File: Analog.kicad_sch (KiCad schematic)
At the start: 18 parts, among them J6 Conn_01x04, U5 LM358

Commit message: cleaned up the whole board
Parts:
- removed C25: 100n, Capacitor_SMD:C_0603_1608Metric_Pad1.08x0.95mm_HandSolder, symbol Device:C_Small
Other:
- moved on the sheet: C24
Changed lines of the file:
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@@
+    (stroke (width 0) (type default))
+  )
+  (wire (pts (xy 184.15 86.36) (xy 184.15 87.63))
+    (stroke (width 0) (type default))
+  )
+  (wire (pts (xy 162.56 143.51) (xy 172.72 143.51))
+    (stroke (width 0) (type default))
+  )
+  (wire (pts (xy 222.25 77.47) (xy 222.25 78.74))
+    (stroke (width 0) (type default))
+  )
+  (wire (pts (xy 189.23 92.71) (xy 187.96 92.71))
+    (stroke (width 0) (type default))
+  )
+  (wire (pts (xy 110.49 149.86) (xy 111.76 149.86))
+    (stroke (width 0) (type default))
+  )
+  (wire (pts (xy 172.72 143.51) (xy 172.72 144.78))
+    (stroke (width 0) (type default))
+  )
+  (wire (pts (xy 69.85 85.09) (xy 74.93 85.09))
+    (stroke (width 0) (type default))
+  )
+  (wire (pts (xy 54.61 85.09) (xy 54.61 86.36))
+    (stroke (width 0) (type default))
+  )
+  (wire (pts (xy 187.96 105.41) (xy 205.74 105.41))
+    (stroke (width 0) (type default))
+  )
+  (wire (pts (xy 162.56 161.29) (xy 172.72 161.29))
+    (stroke (width 0) (type default))
+  )
+  (wire (pts (xy 187.96 92.71) (xy 187.96 105.41))
     (stroke (width 0) (type default))
   )
@@
     (stroke (width 0) (type default))
   )
-  (wire (pts (xy 184.15 86.36) (xy 184.15 87.63))
-    (stroke (width 0) (type default))
-  )
-  (wire (pts (xy 162.56 143.51) (xy 172.72 143.51))
-    (stroke (width 0) (type default))
-  )
-  (wire (pts (xy 154.94 143.51) (xy 162.56 143.51))
-    (stroke (width 0) (type default))
-  )
-  (wire (pts (xy 154.94 161.29) (xy 162.56 161.29))
-    (stroke (width 0) (type default))
-  )
-  (wire (pts (xy 222.25 77.47) (xy 222.25 78.74))
-    (stroke (width 0) (type default))
-  )
-  (wire (pts (xy 189.23 92.71) (xy 187.96 92.71))
-    (stroke (width 0) (type default))
-  )
-  (wire (pts (xy 110.49 149.86) (xy 111.76 149.86))
-    (stroke (width 0) (type default))
-  )
-  (wire (pts (xy 172.72 143.51) (xy 172.72 144.78))
-    (stroke (width 0) (type default))
-  )
-  (wire (pts (xy 69.85 85.09) (xy 74.93 85.09))
-    (stroke (width 0) (type default))
-  )
-  (wire (pts (xy 162.56 143.51) (xy 162.56 149.86))
-    (stroke (width 0) (type default))
-  )
-  (wire (pts (xy 54.61 85.09) (xy 54.61 86.36))
-    (stroke (width 0) (type default))
-  )
-  (wire (pts (xy 187.96 105.41) (xy 205.74 105.41))
-    (stroke (width 0) (type default))
-  )
-  (wire (pts (xy 162.56 161.29) (xy 172.72 161.29))
-    (stroke (width 0) (type default))
-  )
-  (wire (pts (xy 187.96 92.71) (xy 187.96 105.41))
-    (stroke (width 0) (type default))
-  )
-  (wire (pts (xy 154.94 154.94) (xy 154.94 161.29))
-    (stroke (width 0) (type default))
-  )
   (wire (pts (xy 161.29 87.63) (xy 162.56 87.63))
     (stroke (width 0) (type default))
@@
     (stroke (width 0) (type default))
   )
-  (wire (pts (xy 154.94 149.86) (xy 154.94 143.51))
+  (wire (pts (xy 162.56 149.86) (xy 162.56 143.51))
     (stroke (width 0) (type default))
   )
@@
     )
   )
-  (symbol (lib_id "Device:C_Small") (at 154.94 152.4 180) (unit 1)
-    (in_bom yes) (on_board yes) (dnp no)
-    (property "Reference" "C24" (at 156.21 151.13 0)
+  (symbol (lib_id "Device:C_Small") (at 162.56 152.4 180) (unit 1)
+    (in_bom yes) (on_board yes) (dnp no)
+    (property "Reference" "C24" (at 163.83 151.13 0)
       (effects (font (size 1.27 1.27)) (justify right))
     )
-    (property "Value" "100n" (at 156.21 153.67 0)
+    (property "Value" "100n" (at 163.83 153.67 0)
       (effects (font (size 1.27 1.27)) (justify right))
     )
-    (property "Footprint" "Capacitor_SMD:C_0603_1608Metric_Pad1.08x0.95mm_HandSolder" (at 154.94 152.4 0)
-      (effects (font (size 1.27 1.27)) hide)
-    )
-    (property "Datasheet" "~" (at 154.94 152.4 0)
+    (property "Footprint" "Capacitor_SMD:C_0603_1608Metric_Pad1.08x0.95mm_HandSolder" (at 162.56 152.4 0)
+      (effects (font (size 1.27 1.27)) hide)
+    )
+    (property "Datasheet" "~" (at 162.56 152.4 0)
       (effects (font (size 1.27 1.27)) hide)
     )
@@
         )
       )
-    )
-  )
-  (symbol (lib_id "Device:C_Small") (at 162.56 152.4 0) (unit 1)
-    (in_bom yes) (on_board yes) (dnp no) (fields_autoplaced)
-    (property "Reference" "C25" (at 165.1 151.1362 0)
-      (effects (font (size 1.27 1.27)) (justify left))
-    )
-    (property "Value" "100n" (at 165.1 153.6762 0)
-      (effects (font (size 1.27 1.27)) (justify left))
-    )
-    (property "Footprint" "Capacitor_SMD:C_0603_1608Metric_Pad1.08x0.95mm_HandSolder" (at 162.56 152.4 0)
-      (effects (font (size 1.27 1.27)) hide)
-    )
-    (property "Datasheet" "~" (at 162.56 152.4 0)
-      (effects (font (size 1.27 1.27)) hide)
-    )
-    (pin "1")
-    (pin "2")
-    (instances
-      (project "Apollo - DSP"
-        (path "/e63e39d7-6ac0-4ffd-8aa3-1841a4541b55/b09314ce-9d59-4e3d-844f-f36b76e34219"
-          (reference "C25") (unit 1)
-        )
-      )

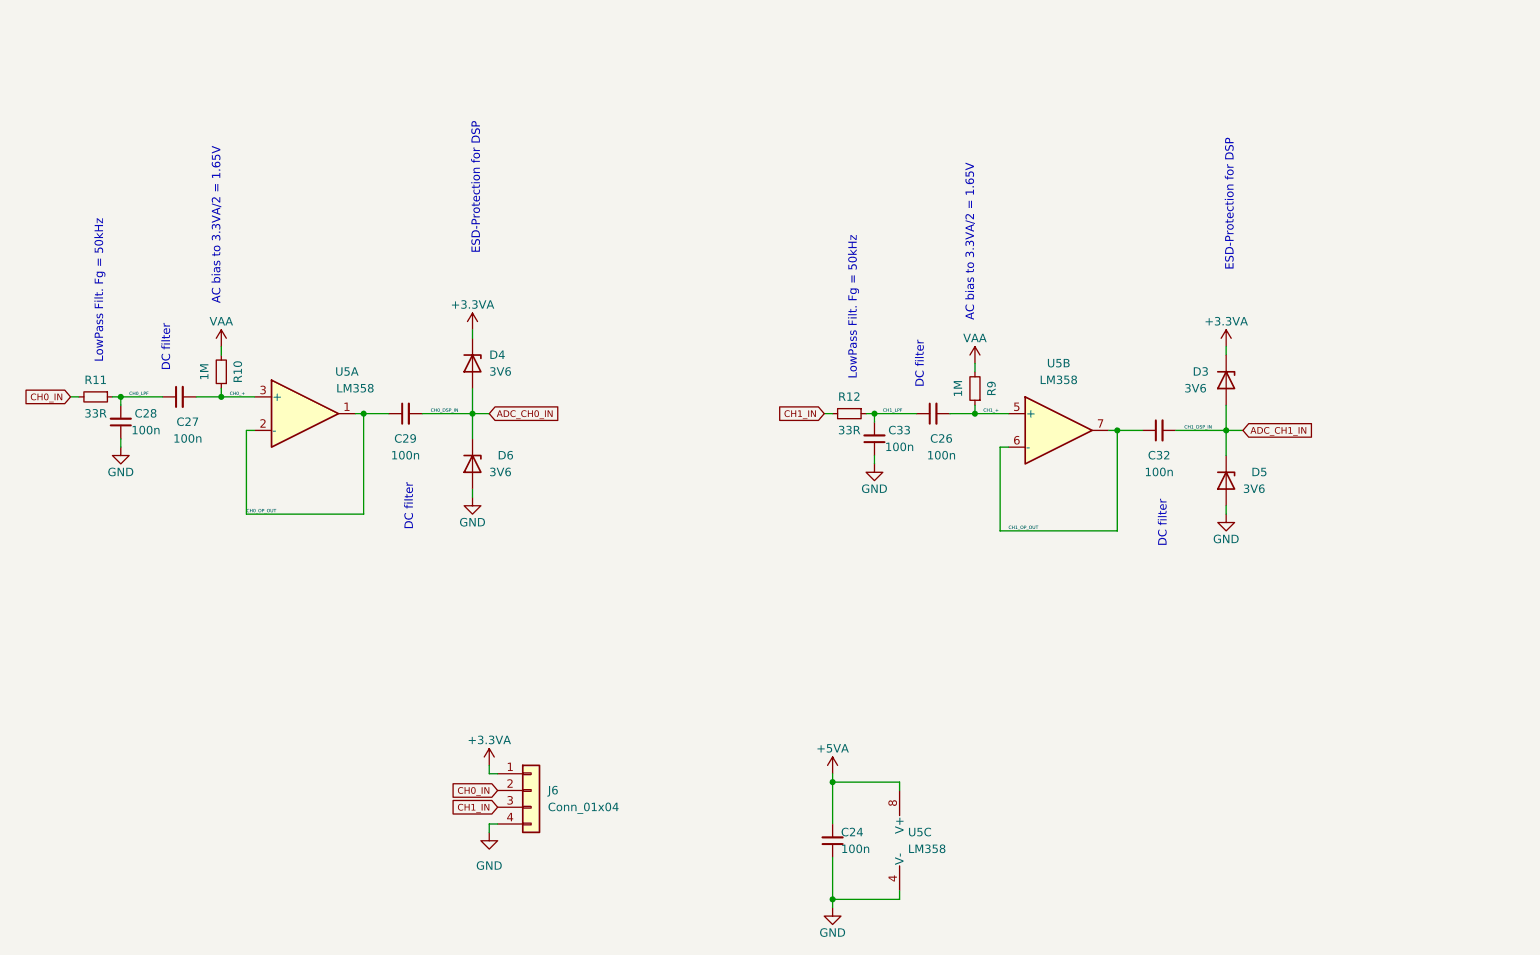
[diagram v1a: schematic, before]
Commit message: made analog circuitry a bit more compact moved whole board
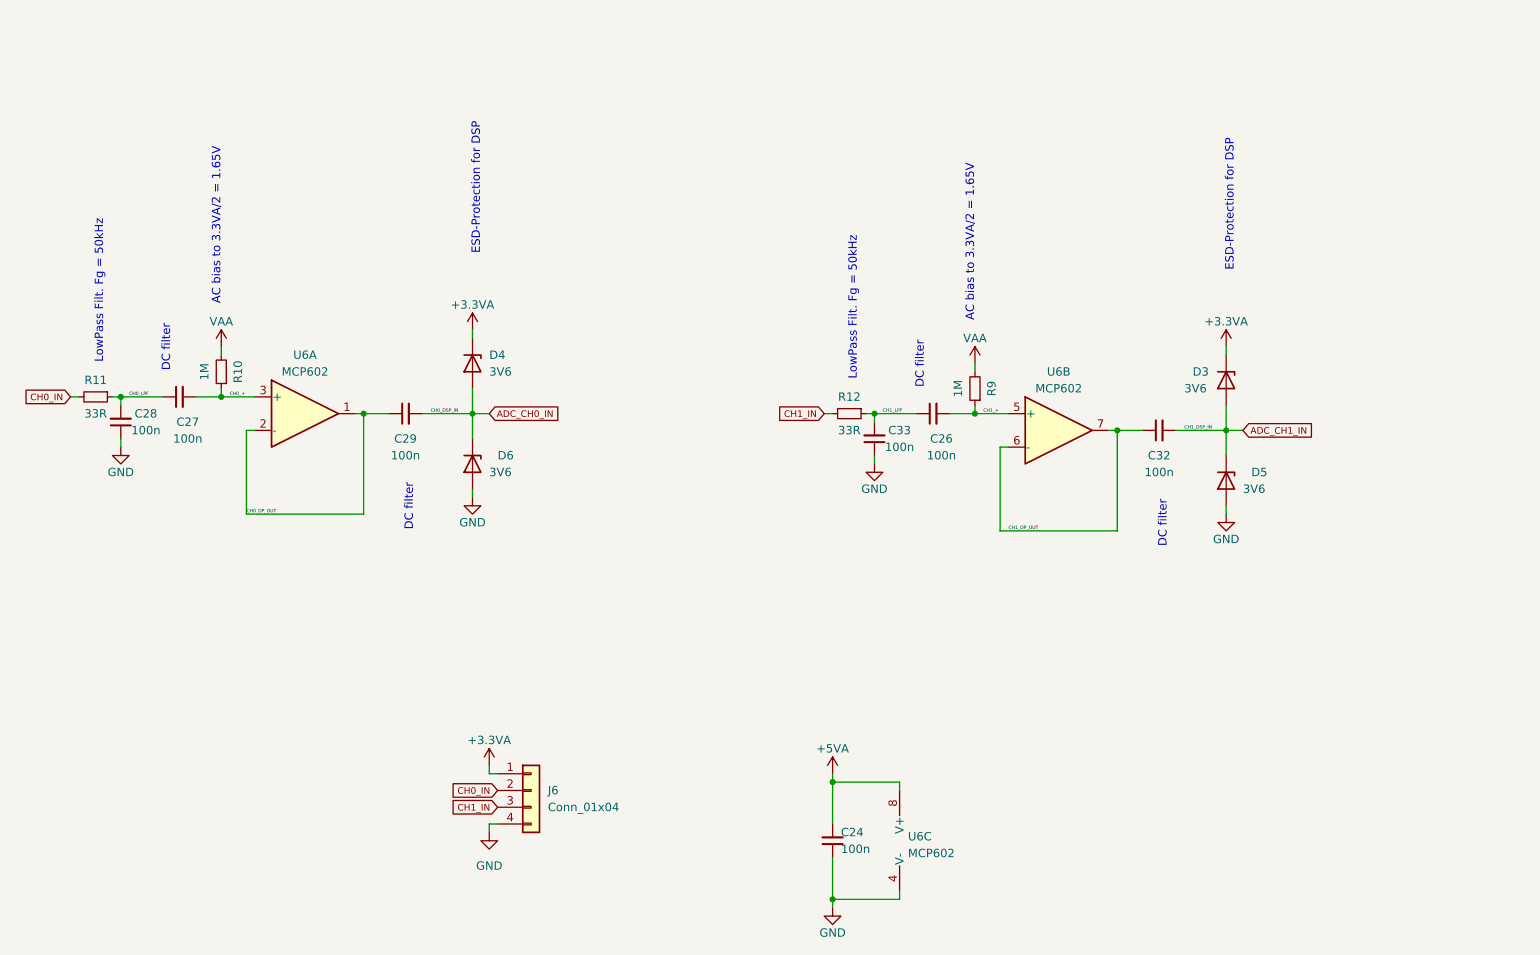
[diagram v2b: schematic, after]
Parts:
- removed U5: LM358, Package_SO:SOIC-8_3.9x4.9mm_P1.27mm, symbol Amplifier_Operational:LM358
- added U6: MCP602, Package_SO:SOIC-8_3.9x4.9mm_P1.27mm, symbol Amplifier_Operational:MCP602
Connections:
- net +5VA: now also U6.8 (V+)
- net CH0_+: now also U6.3 (+)
- net CH0_OP_OUT: now also U6.1, U6.2 (-)
- net CH1_+: now also U6.5 (+)
- net CH1_OP_OUT: now also U6.6 (-), U6.7
- net GND: now also U6.4 (V-)

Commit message: added sram chip again, might come in handy for mor complex calculations
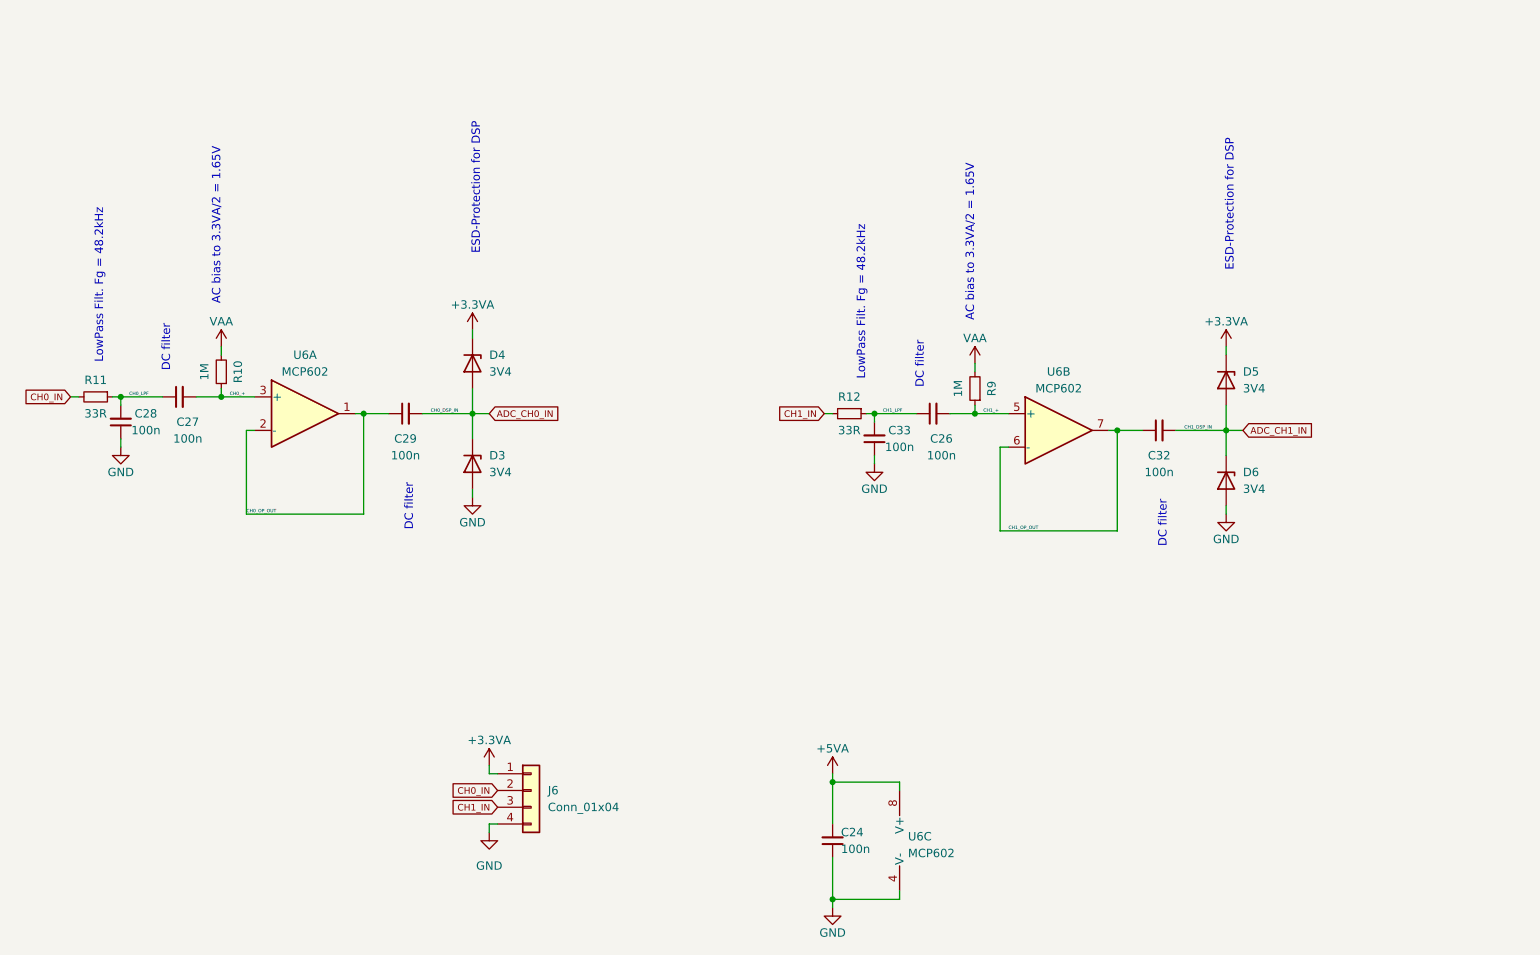
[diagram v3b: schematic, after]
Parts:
- D3, D4, D5, D6: value 3V6 -> 3V4; footprint Resistor_SMD:R_0603_1608Metric_Pad0.98x0.95mm_HandSolder -> Diode_SMD:D_SOD-123F
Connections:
- net +3.3VA: now also D5.1 (K); no longer D3.1 (K)
- net ADC_CH0_IN: now also D3.1 (K); no longer D6.1 (K)
- net ADC_CH1_IN: now also D5.2 (A), D6.1 (K); no longer D3.2 (A), D5.1 (K)
- net GND: now also D3.2 (A); no longer D5.2 (A)
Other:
- note added: "LowPass Filt. Fg = 48.2kHz"
- note removed: "LowPass Filt. Fg = 50kHz"
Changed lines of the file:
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@@
+    (effects (font (size 1.27 1.27)) (justify left bottom))
+  )
+  (text "LowPass Filt. Fg = 48.2kHz" (at 167.64 82.55 90)
     (effects (font (size 1.27 1.27)) (justify left bottom))
   )
@@
     (effects (font (size 1.27 1.27)) (justify left bottom))
   )
-  (text "LowPass Filt. Fg = 50kHz" (at 52.07 80.01 90)
+  (text "LowPass Filt. Fg = 48.2kHz" (at 52.07 80.01 90)
     (effects (font (size 1.27 1.27)) (justify left bottom))
   )
   (text "AC bias to 3.3VA/2 = 1.65V\n" (at 184.15 73.66 90)
-    (effects (font (size 1.27 1.27)) (justify left bottom))
-  )
-  (text "LowPass Filt. Fg = 50kHz" (at 166.37 82.55 90)
     (effects (font (size 1.27 1.27)) (justify left bottom))
   )
@@
         (path "/e63e39d7-6ac0-4ffd-8aa3-1841a4541b55/b09314ce-9d59-4e3d-844f-f36b76e34219"
           (reference "#PWR0154") (unit 1)
+        )
+      )
+    )
+  )
+  (symbol (lib_id "Device:D_Zener") (at 222.25 97.79 270) (unit 1)
+    (in_bom yes) (on_board yes) (dnp no)
+    (property "Reference" "D6" (at 224.79 96.52 90)
+      (effects (font (size 1.27 1.27)) (justify left))
+    )
+    (property "Value" "3V4" (at 224.79 99.06 90)
+      (effects (font (size 1.27 1.27)) (justify left))
+    )
+    (property "Footprint" "Diode_SMD:D_SOD-123F" (at 222.25 97.79 0)
+      (effects (font (size 1.27 1.27)) hide)
+    )
+    (property "Datasheet" "~" (at 222.25 97.79 0)
+      (effects (font (size 1.27 1.27)) hide)
+    )
+    (pin "1")
+    (pin "2")
+    (instances
+      (project "Apollo - DSP"
+        (path "/e63e39d7-6ac0-4ffd-8aa3-1841a4541b55/b09314ce-9d59-4e3d-844f-f36b76e34219"
+          (reference "D6") (unit 1)
         )
       )
@@
     )
   )
+  (symbol (lib_id "Device:D_Zener") (at 107.95 95.25 270) (unit 1)
+    (in_bom yes) (on_board yes) (dnp no)
+    (property "Reference" "D3" (at 110.49 93.98 90)
+      (effects (font (size 1.27 1.27)) (justify left))
+    )
+    (property "Value" "3V4" (at 110.49 96.52 90)
+      (effects (font (size 1.27 1.27)) (justify left))
+    )
+    (property "Footprint" "Diode_SMD:D_SOD-123F" (at 107.95 95.25 0)
+      (effects (font (size 1.27 1.27)) hide)
+    )
+    (property "Datasheet" "~" (at 107.95 95.25 0)
+      (effects (font (size 1.27 1.27)) hide)
+    )
+    (pin "1")
+    (pin "2")
+    (instances
+      (project "Apollo - DSP"
+        (path "/e63e39d7-6ac0-4ffd-8aa3-1841a4541b55/b09314ce-9d59-4e3d-844f-f36b76e34219"
+          (reference "D3") (unit 1)
+        )
+      )
+    )
+  )
   (symbol (lib_id "power:+5VA") (at 162.56 142.24 0) (unit 1)
     (in_bom yes) (on_board yes) (dnp no)
@@
     )
   )
+  (symbol (lib_id "Device:D_Zener") (at 222.25 82.55 270) (unit 1)
+    (in_bom yes) (on_board yes) (dnp no)
+    (property "Reference" "D5" (at 224.79 81.28 90)
+      (effects (font (size 1.27 1.27)) (justify left))
+    )
+    (property "Value" "3V4" (at 224.79 83.82 90)
+      (effects (font (size 1.27 1.27)) (justify left))
+    )
+    (property "Footprint" "Diode_SMD:D_SOD-123F" (at 222.25 82.55 0)
+      (effects (font (size 1.27 1.27)) hide)
+    )
+    (property "Datasheet" "~" (at 222.25 82.55 0)
+      (effects (font (size 1.27 1.27)) hide)
+    )
+    (pin "1")
+    (pin "2")
+    (instances
+      (project "Apollo - DSP"
+        (path "/e63e39d7-6ac0-4ffd-8aa3-1841a4541b55/b09314ce-9d59-4e3d-844f-f36b76e34219"
+          (reference "D5") (unit 1)
+        )
+      )
+    )
+  )
   (symbol (lib_id "power:GND") (at 168.91 95.25 0) (unit 1)
     (in_bom yes) (on_board yes) (dnp no)
@@
         (path "/e63e39d7-6ac0-4ffd-8aa3-1841a4541b55/b09314ce-9d59-4e3d-844f-f36b76e34219"
           (reference "#PWR0164") (unit 1)
-        )
-      )
-    )
-  )
-  (symbol (lib_id "Device:D_Zener") (at 222.25 82.55 270) (unit 1)
-    (in_bom yes) (on_board yes) (dnp no)
-    (property "Reference" "D3" (at 217.17 81.28 90)
-      (effects (font (size 1.27 1.27)) (justify left))
-    )
-    (property "Value" "3V6" (at 215.9 83.82 90)
-      (effects (font (size 1.27 1.27)) (justify left))
-    )
-    (property "Footprint" "Resistor_SMD:R_0603_1608Metric_Pad0.98x0.95mm_HandSolder" (at 222.25 82.55 0)
-      (effects (font (size 1.27 1.27)) hide)
-    )
-    (property "Datasheet" "~" (at 222.25 82.55 0)
-      (effects (font (size 1.27 1.27)) hide)
-    )
-    (pin "1")
-    (pin "2")
-    (instances
-      (project "Apollo - DSP"
-        (path "/e63e39d7-6ac0-4ffd-8aa3-1841a4541b55/b09314ce-9d59-4e3d-844f-f36b76e34219"
-          (reference "D3") (unit 1)
         )
       )
@@
         (path "/e63e39d7-6ac0-4ffd-8aa3-1841a4541b55/b09314ce-9d59-4e3d-844f-f36b76e34219"
           (reference "C27") (unit 1)
-        )
-      )
-    )
-  )
-  (symbol (lib_id "Device:D_Zener") (at 222.25 97.79 270) (unit 1)
-    (in_bom yes) (on_board yes) (dnp no)
-    (property "Reference" "D5" (at 226.06 96.52 90)
-      (effects (font (size 1.27 1.27)) (justify left))
-    )
-    (property "Value" "3V6" (at 224.79 99.06 90)
-      (effects (font (size 1.27 1.27)) (justify left))
-    )
-    (property "Footprint" "Resistor_SMD:R_0603_1608Metric_Pad0.98x0.95mm_HandSolder" (at 222.25 97.79 0)
-      (effects (font (size 1.27 1.27)) hide)
-    )
-    (property "Datasheet" "~" (at 222.25 97.79 0)
-      (effects (font (size 1.27 1.27)) hide)
-    )
-    (pin "1")
-    (pin "2")
-    (instances
-      (project "Apollo - DSP"
-        (path "/e63e39d7-6ac0-4ffd-8aa3-1841a4541b55/b09314ce-9d59-4e3d-844f-f36b76e34219"
-          (reference "D5") (unit 1)
         )
       )
@@
       (effects (font (size 1.27 1.27)) (justify left))
     )
-    (property "Value" "3V6" (at 110.49 81.28 90)
-      (effects (font (size 1.27 1.27)) (justify left))
-    )
-    (property "Footprint" "Resistor_SMD:R_0603_1608Metric_Pad0.98x0.95mm_HandSolder" (at 107.95 80.01 0)
+    (property "Value" "3V4" (at 110.49 81.28 90)
+      (effects (font (size 1.27 1.27)) (justify left))
+    )
+    (property "Footprint" "Diode_SMD:D_SOD-123F" (at 107.95 80.01 0)
       (effects (font (size 1.27 1.27)) hide)
     )
@@
         )
       )
-    )
-  )
-  (symbol (lib_id "Device:D_Zener") (at 107.95 95.25 270) (unit 1)
-    (in_bom yes) (on_board yes) (dnp no)
-    (property "Reference" "D6" (at 111.76 93.98 90)
-      (effects (font (size 1.27 1.27)) (justify left))
-    )
-    (property "Value" "3V6" (at 110.49 96.52 90)
-      (effects (font (size 1.27 1.27)) (justify left))
-    )
-    (property "Footprint" "Resistor_SMD:R_0603_1608Metric_Pad0.98x0.95mm_HandSolder" (at 107.95 95.25 0)
-      (effects (font (size 1.27 1.27)) hide)
-    )
-    (property "Datasheet" "~" (at 107.95 95.25 0)
-      (effects (font (size 1.27 1.27)) hide)
-    )
-    (pin "1")
-    (pin "2")
-    (instances
-      (project "Apollo - DSP"
-        (path "/e63e39d7-6ac0-4ffd-8aa3-1841a4541b55/b09314ce-9d59-4e3d-844f-f36b76e34219"
-          (reference "D6") (unit 1)
-        )
-      )
